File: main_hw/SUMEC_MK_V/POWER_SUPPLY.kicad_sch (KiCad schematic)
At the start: 40 parts, among them IC1 TPS565242DRLR, J1 XT30PW-M, Q1 Q_PMOS, Q2 Q_PMOS, SW1 SW_DPDT_x2, U1 INA226, U2 TPS62133, U3 AP62301Z6

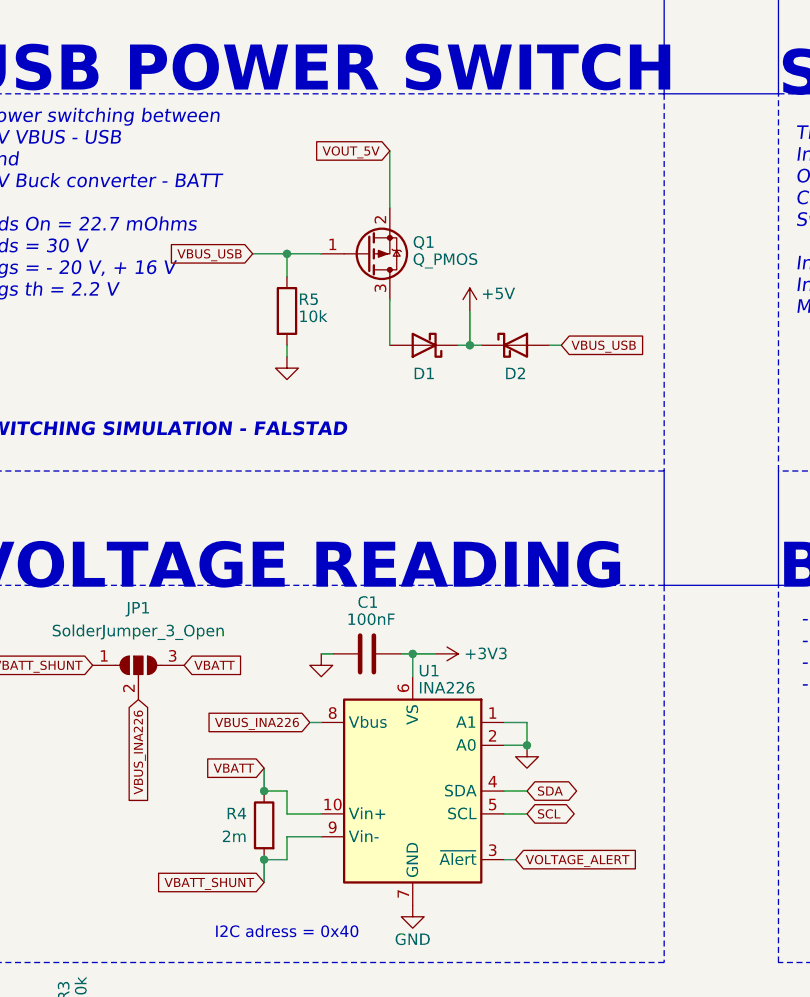
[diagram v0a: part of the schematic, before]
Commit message: PCB Update, signal routing
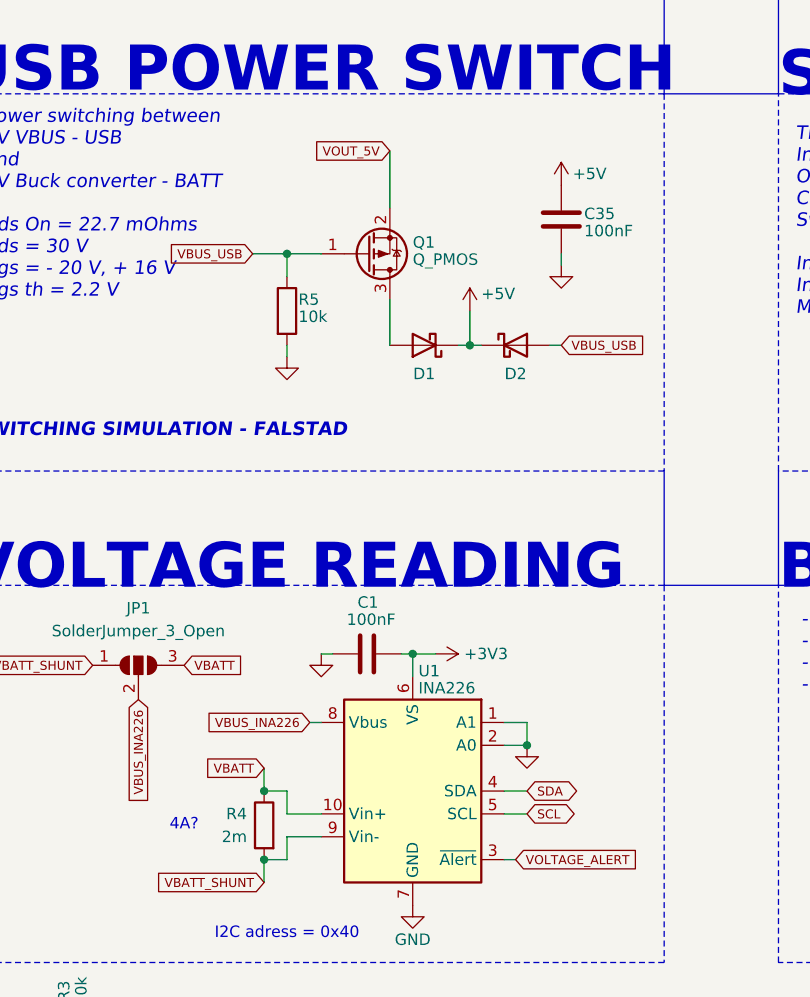
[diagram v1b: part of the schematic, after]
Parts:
- added C35: 100nF, Capacitor_SMD:C_0805_2012Metric_Pad1.18x1.45mm_HandSolder, symbol Device:C
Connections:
- net +5V: now also C35.1
- net GND: now also C35.2
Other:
- note added: "4A?"

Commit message: PCB routing update
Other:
- note added: "will 0805 resistor be sufficent?"

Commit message: a lot of routing and layout updates
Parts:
- removed C10: 22uF, Capacitor_Tantalum_SMD:CP_EIA-2012-12_Kemet-R_Pad1.30x1.05mm_HandSolder, symbol Device:C_Polarized
- removed C2: 3.3nF, Capacitor_SMD:C_0805_2012Metric_Pad1.18x1.45mm_HandSolder, symbol Device:C
- removed C4: 10uF, Capacitor_Tantalum_SMD:CP_EIA-3216-18_Kemet-A_Pad1.58x1.35mm_HandSolder, symbol Device:C_Polarized
- removed C6: 100nF, Capacitor_SMD:C_0805_2012Metric_Pad1.18x1.45mm_HandSolder, symbol Device:C
- removed L2: 2.2uH, Inductor_SMD:L_Vishay_IHLP-1616, symbol Device:L
- removed R9: 100k, Resistor_SMD:R_0805_2012Metric_Pad1.20x1.40mm_HandSolder, symbol Device:R
- removed U2: TPS62133, Package_DFN_QFN:VQFN-16-1EP_3x3mm_P0.5mm_EP1.68x1.68mm_ThermalVias, symbol Regulator_Switching:TPS62133
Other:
- moved on the sheet: C12, C13, C14, C15, L3, R10, R11, R12, R13, U3

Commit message: sumec pcb update
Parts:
- renumbered C9 to C10, C15 to C11, C11 to C12, C35 to C2, C12 to C3, C3 to C4, C13 to C6, C14 to C9, L3 to L2, R3 to R1, R13 to R10, R4 to R2, R5 to R3, R6 to R4, R7 to R5, R10 to R6, R11 to R7, R12 to R9, U3 to U2
